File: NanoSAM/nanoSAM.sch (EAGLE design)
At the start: 90 parts, among them IC3 AD5241, J1 POWER_JACK, U1 LTC3260EMSEPBF

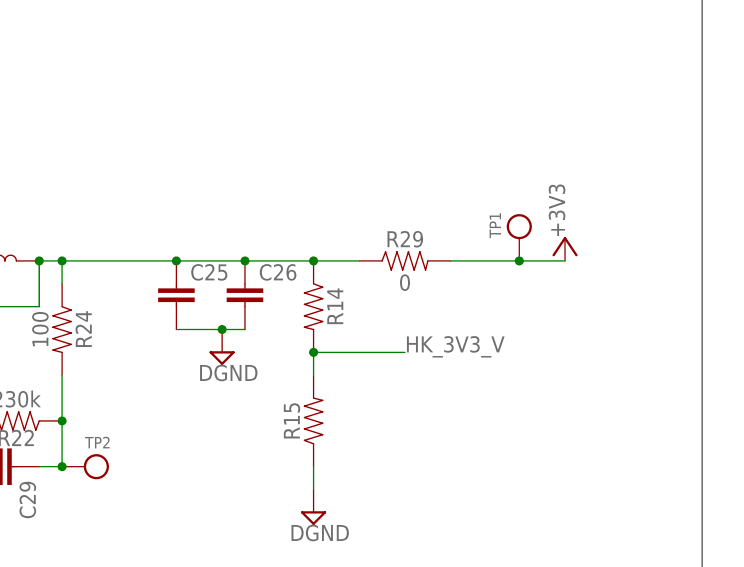
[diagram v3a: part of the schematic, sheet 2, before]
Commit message: routed +3v3 power supply
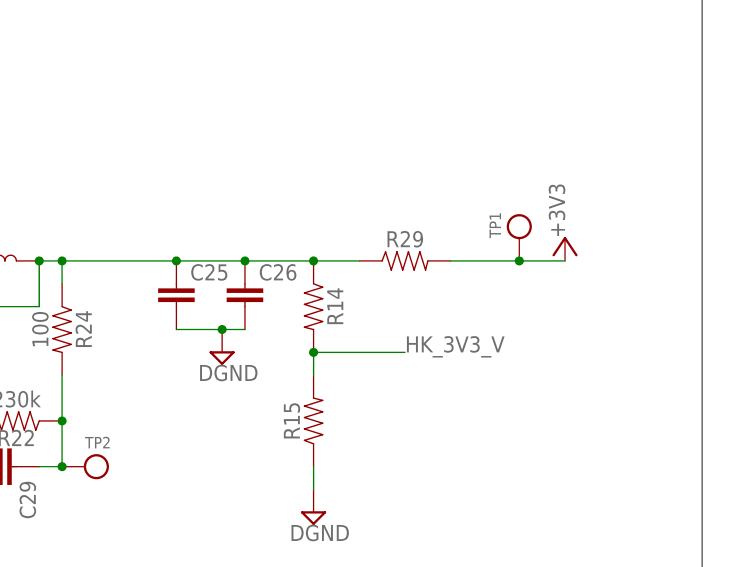
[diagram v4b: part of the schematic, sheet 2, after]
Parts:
- R29: value 0 -> (none); device SparkFun-Resistors:RESISTOR0603 -> SparkFun-Resistors:RESISTOR1206
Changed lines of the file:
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@@
 <?xml version="1.0" encoding="utf-8"?>
 <!DOCTYPE eagle SYSTEM "eagle.dtd">
-<eagle version="9.5.1">
+<eagle version="9.3.0">
 <drawing>
 <settings>
@@
 <grid distance="0.1" unitdist="inch" unit="inch" style="lines" multiple="1" display="no" altdistance="0.01" altunitdist="inch" altunit="inch"/>
 <layers>
-<layer number="1" name="Top" color="4" fill="1" visible="no" active="no"/>
-<layer number="2" name="Route2" color="16" fill="1" visible="no" active="no"/>
-<layer number="3" name="Route3" color="17" fill="1" visible="no" active="no"/>
-<layer number="4" name="Route4" color="18" fill="1" visible="no" active="no"/>
-<layer number="5" name="Route5" color="19" fill="1" visible="no" active="no"/>
-<layer number="6" name="Route6" color="25" fill="1" visible="no" active="no"/>
-<layer number="7" name="Route7" color="26" fill="1" visible="no" active="no"/>
-<layer number="8" name="Route8" color="27" fill="1" visible="no" active="no"/>
-<layer number="9" name="Route9" color="28" fill="1" visible="no" active="no"/>
-<layer number="10" name="Route10" color="29" fill="1" visible="no" active="no"/>
-<layer number="11" name="Route11" color="30" fill="1" visible="no" active="no"/>
-<layer number="12" name="Route12" color="20" fill="1" visible="no" active="no"/>
-<layer number="13" name="Route13" color="21" fill="1" visible="no" active="no"/>
-<layer number="14" name="Route14" color="22" fill="1" visible="no" active="no"/>
-<layer number="15" name="Route15" color="23" fill="1" visible="no" active="no"/>
-<layer number="16" name="Bottom" color="1" fill="1" visible="no" active="no"/>
-<layer number="17" name="Pads" color="2" fill="1" visible="no" active="no"/>
-<layer number="18" name="Vias" color="2" fill="1" visible="no" active="no"/>
-<layer number="19" name="Unrouted" color="6" fill="1" visible="no" active="no"/>
-<layer number="20" name="Dimension" color="24" fill="1" visible="no" active="no"/>
-<layer number="21" name="tPlace" color="7" fill="1" visible="no" active="no"/>
-<layer number="22" name="bPlace" color="7" fill="1" visible="no" active="no"/>
-<layer number="23" name="tOrigins" color="15" fill="1" visible="no" active="no"/>
-<layer number="24" name="bOrigins" color="15" fill="1" visible="no" active="no"/>
-<layer number="25" name="tNames" color="7" fill="1" visible="no" active="no"/>
-<layer number="26" name="bNames" color="7" fill="1" visible="no" active="no"/>
-<layer number="27" name="tValues" color="7" fill="1" visible="no" active="no"/>
-<layer number="28" name="bValues" color="7" fill="1" visible="no" active="no"/>
+<layer number="1" name="Top" color="4" fill="1" visible="yes" active="no"/>
+<layer number="2" name="Route2" color="16" fill="1" visible="yes" active="no"/>
+<layer number="3" name="Route3" color="17" fill="1" visible="yes" active="no"/>
+<layer number="4" name="Route4" color="18" fill="1" visible="yes" active="no"/>
+<layer number="5" name="Route5" color="19" fill="1" visible="yes" active="no"/>
+<layer number="6" name="Route6" color="25" fill="1" visible="yes" active="no"/>
+<layer number="7" name="Route7" color="26" fill="1" visible="yes" active="no"/>
+<layer number="8" name="Route8" color="27" fill="1" visible="yes" active="no"/>
+<layer number="9" name="Route9" color="28" fill="1" visible="yes" active="no"/>
+<layer number="10" name="Route10" color="29" fill="1" visible="yes" active="no"/>
+<layer number="11" name="Route11" color="30" fill="1" visible="yes" active="no"/>
+<layer number="12" name="Route12" color="20" fill="1" visible="yes" active="no"/>
+<layer number="13" name="Route13" color="21" fill="1" visible="yes" active="no"/>
+<layer number="14" name="Route14" color="22" fill="1" visible="yes" active="no"/>
+<layer number="15" name="Route15" color="23" fill="1" visible="yes" active="no"/>
+<layer number="16" name="Bottom" color="1" fill="1" visible="yes" active="no"/>
+<layer number="17" name="Pads" color="2" fill="1" visible="yes" active="no"/>
+<layer number="18" name="Vias" color="2" fill="1" visible="yes" active="no"/>
+<layer number="19" name="Unrouted" color="6" fill="1" visible="yes" active="no"/>
+<layer number="20" name="Dimension" color="24" fill="1" visible="yes" active="no"/>
+<layer number="21" name="tPlace" color="7" fill="1" visible="yes" active="no"/>
+<layer number="22" name="bPlace" color="7" fill="1" visible="yes" active="no"/>
+<layer number="23" name="tOrigins" color="15" fill="1" visible="yes" active="no"/>
+<layer number="24" name="bOrigins" color="15" fill="1" visible="yes" active="no"/>
+<layer number="25" name="tNames" color="7" fill="1" visible="yes" active="no"/>
+<layer number="26" name="bNames" color="7" fill="1" visible="yes" active="no"/>
+<layer number="27" name="tValues" color="7" fill="1" visible="yes" active="no"/>
+<layer number="28" name="bValues" color="7" fill="1" visible="yes" active="no"/>
 <layer number="29" name="tStop" color="7" fill="3" visible="no" active="no"/>
 <layer number="30" name="bStop" color="7" fill="6" visible="no" active="no"/>
@@
 <layer number="35" name="tGlue" color="7" fill="4" visible="no" active="no"/>
 <layer number="36" name="bGlue" color="7" fill="5" visible="no" active="no"/>
-<layer number="37" name="tTest" color="7" fill="1" visible="no" active="no"/>
-<layer number="38" name="bTest" color="7" fill="1" visible="no" active="no"/>
+<layer number="37" name="tTest" color="7" fill="1" visible="yes" active="no"/>
+<layer number="38" name="bTest" color="7" fill="1" visible="yes" active="no"/>
 <layer number="39" name="tKeepout" color="4" fill="11" visible="no" active="no"/>
 <layer number="40" name="bKeepout" color="1" fill="11" visible="no" active="no"/>
@@
 <layer number="44" name="Drills" color="7" fill="1" visible="no" active="no"/>
 <layer number="45" name="Holes" color="7" fill="1" visible="no" active="no"/>
-<layer number="46" name="Milling" color="3" fill="1" visible="no" active="no"/>
-<layer number="47" name="Measures" color="7" fill="1" visible="no" active="no"/>
-<layer number="48" name="Document" color="7" fill="1" visible="no" active="no"/>
-<layer number="49" name="Reference" color="7" fill="1" visible="no" active="no"/>
-<layer number="50" name="dxf" color="7" fill="1" visible="no" active="no"/>
-<layer number="51" name="tDocu" color="7" fill="1" visible="no" active="no"/>
-<layer number="52" name="bDocu" color="7" fill="1" visible="no" active="no"/>
-<layer number="53" name="tGND_GNDA" color="7" fill="9" visible="no" active="no"/>
-<layer number="54" name="bGND_GNDA" color="1" fill="9" visible="no" active="no"/>
-<layer number="56" name="wert" color="7" fill="1" visible="no" active="no"/>
-<layer number="57" name="tCAD" color="7" fill="1" visible="no" active="no"/>
-<layer number="59" name="tCarbon" color="7" fill="1" visible="no" active="no"/>
-<layer number="60" name="bCarbon" color="7" fill="1" visible="no" active="no"/>
+<layer number="46" name="Milling" color="3" fill="1" visible="yes" active="no"/>
+<layer number="47" name="Measures" color="7" fill="1" visible="yes" active="no"/>
+<layer number="48" name="Document" color="7" fill="1" visible="yes" active="no"/>
+<layer number="49" name="Reference" color="7" fill="1" visible="yes" active="no"/>
+<layer number="50" name="dxf" color="7" fill="1" visible="yes" active="no"/>
+<layer number="51" name="tDocu" color="7" fill="1" visible="yes" active="no"/>
+<layer number="52" name="bDocu" color="7" fill="1" visible="yes" active="no"/>
+<layer number="53" name="tGND_GNDA" color="7" fill="9" visible="yes" active="no"/>
+<layer number="54" name="bGND_GNDA" color="1" fill="9" visible="yes" active="no"/>
+<layer number="56" name="wert" color="7" fill="1" visible="yes" active="no"/>
+<layer number="57" name="tCAD" color="7" fill="1" visible="yes" active="no"/>
+<layer number="59" name="tCarbon" color="7" fill="1" visible="yes" active="no"/>
+<layer number="60" name="bCarbon" color="7" fill="1" visible="yes" active="no"/>
 <layer number="88" name="SimResults" color="9" fill="1" visible="yes" active="yes"/>
 <layer number="89" name="SimProbes" color="9" fill="1" visible="yes" active="yes"/>
@@
 <part name="R27" library="SparkFun-Resistors" library_urn="urn:adsk.eagle:library:532" deviceset="RESISTOR" device="0603" package3d_urn="urn:adsk.eagle:package:39650/1" value="0"/>
 <part name="TP1" library="testpoint" deviceset="TESTPOINT" device=""/>
-<part name="R29" library="SparkFun-Resistors" library_urn="urn:adsk.eagle:library:532" deviceset="RESISTOR" device="0603" package3d_urn="urn:adsk.eagle:package:39650/1" value="0"/>
+<part name="R29" library="SparkFun-Resistors" library_urn="urn:adsk.eagle:library:532" deviceset="RESISTOR" device="1206" package3d_urn="urn:adsk.eagle:package:39654/1" value=" "/>
 <part name="J1" library="SparkFun-Connectors" library_urn="urn:adsk.eagle:library:513" deviceset="POWER_JACK" device="" package3d_urn="urn:adsk.eagle:package:38231/1"/>
 <part name="SUPPLY18" library="supply2" library_urn="urn:adsk.eagle:library:372" deviceset="DGND" device=""/>

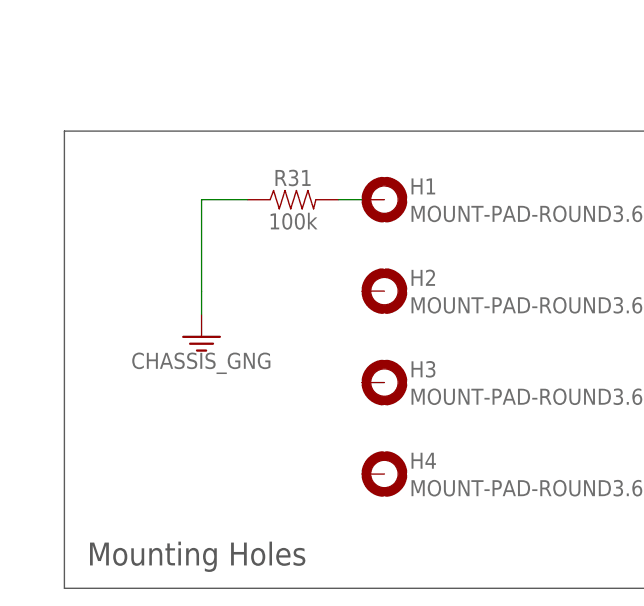
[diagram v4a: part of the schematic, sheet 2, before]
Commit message: Finished part placements and bus wiring
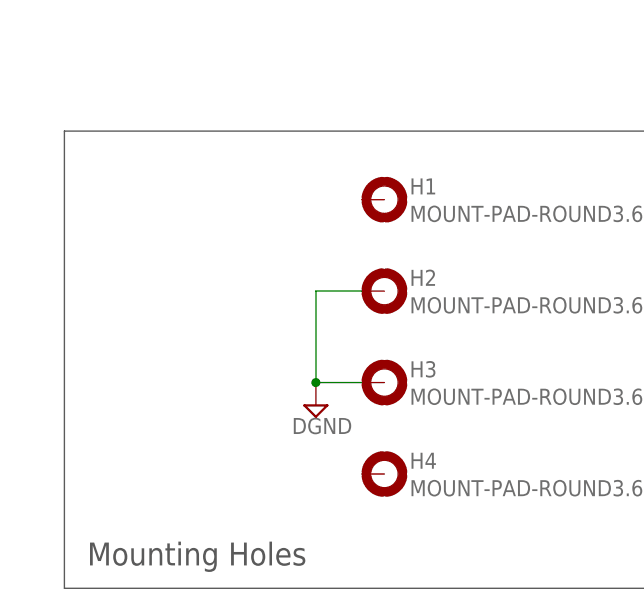
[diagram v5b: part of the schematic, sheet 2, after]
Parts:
- removed R31: 100k, SparkFun-Resistors:RESISTOR1206
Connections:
- removed net CHASSIS: R31.1
- removed net GND: R19.1, U$4.3, U$4.P$7, U$4.P$8, U$4.V-
- removed net N$30: H1.MOUNT, R31.2
- removed net VNEG: U$1.P$2, U$3.V-
- net -5V: now also U$1.P$2, U$3.V-
- net DGND: now also H2.MOUNT, H3.MOUNT, R19.1, U$4.3, U$4.P$7, U$4.P$8, U$4.V-
- net FLASH_CS1: now also U$2.D8; no longer U$2.D9
- net FLASH_CS2: now also U$2.D9; no longer U$2.D8

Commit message: fixed some DRC errors
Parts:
- removed C4: 0.1uF, SparkFun-Capacitors:0.1UF-0603-25V-5%
- removed IC3: AD5241, AD5241:AD5241
- removed R1, R5: (no value), SparkFun-Resistors:RESISTOR0805
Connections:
- removed net GAIN_SCL: IC3.SCL, U$2.D19/A5
- removed net GAIN_SDA: IC3.SDA, U$2.D18/A4
- removed net N$5: IC3.VDD, R1.1
- removed net N$9: IC3.!SHDN, R5.2
- net +3V3: no longer C4.1, R1.2, R5.1
- net DGND: no longer C4.2, IC3.AD0, IC3.AD1, IC3.GND, IC3.NC, IC3.VSS
- net N$1: no longer IC3.W
- net N$2: no longer IC3.A
